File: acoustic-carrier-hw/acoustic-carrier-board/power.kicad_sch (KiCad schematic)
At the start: 73 parts, among them J201 Conn_02x06_Odd_Even, Q201 AO3401A, U201 TPS2121RUX, U202 TLV62569DBV, U203 TLV62569DBV, U204 TLV62569DBV, U205 TLV62569DBV, U206 OPA376xxDBV

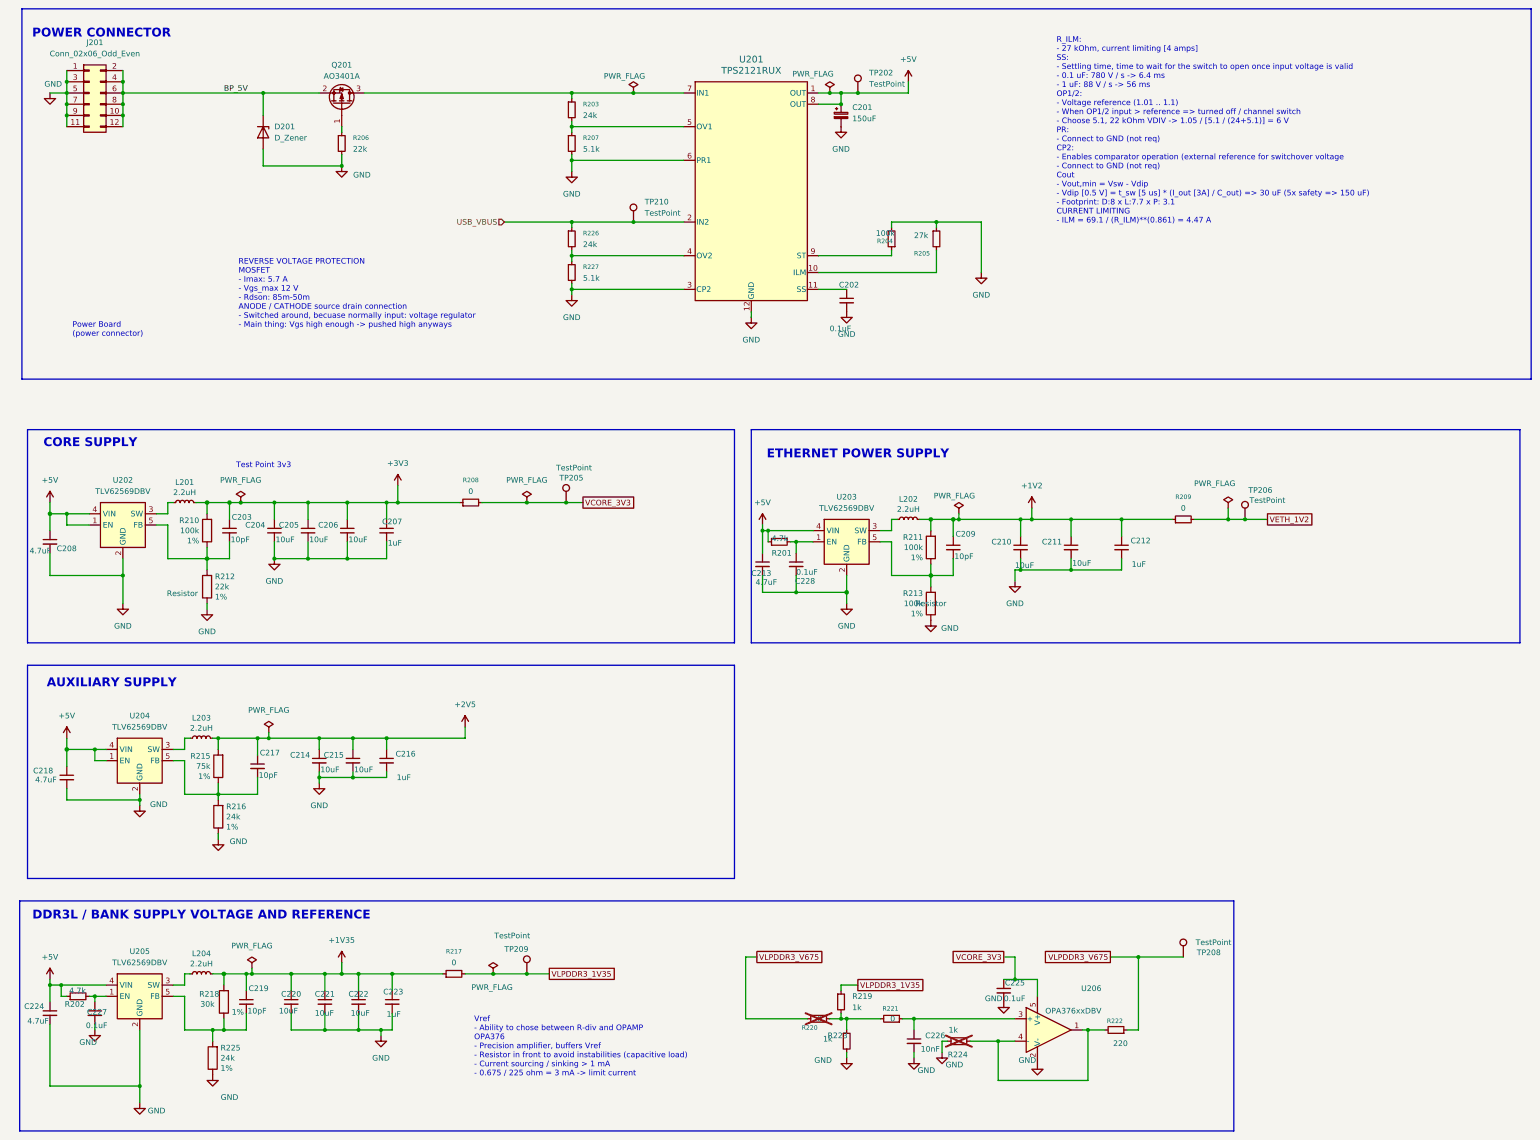
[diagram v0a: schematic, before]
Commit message: [carrier] finished for production (next) reroute the LPDDR3, with appropriate CMD-CTRL bus delays, and change banks for command-control
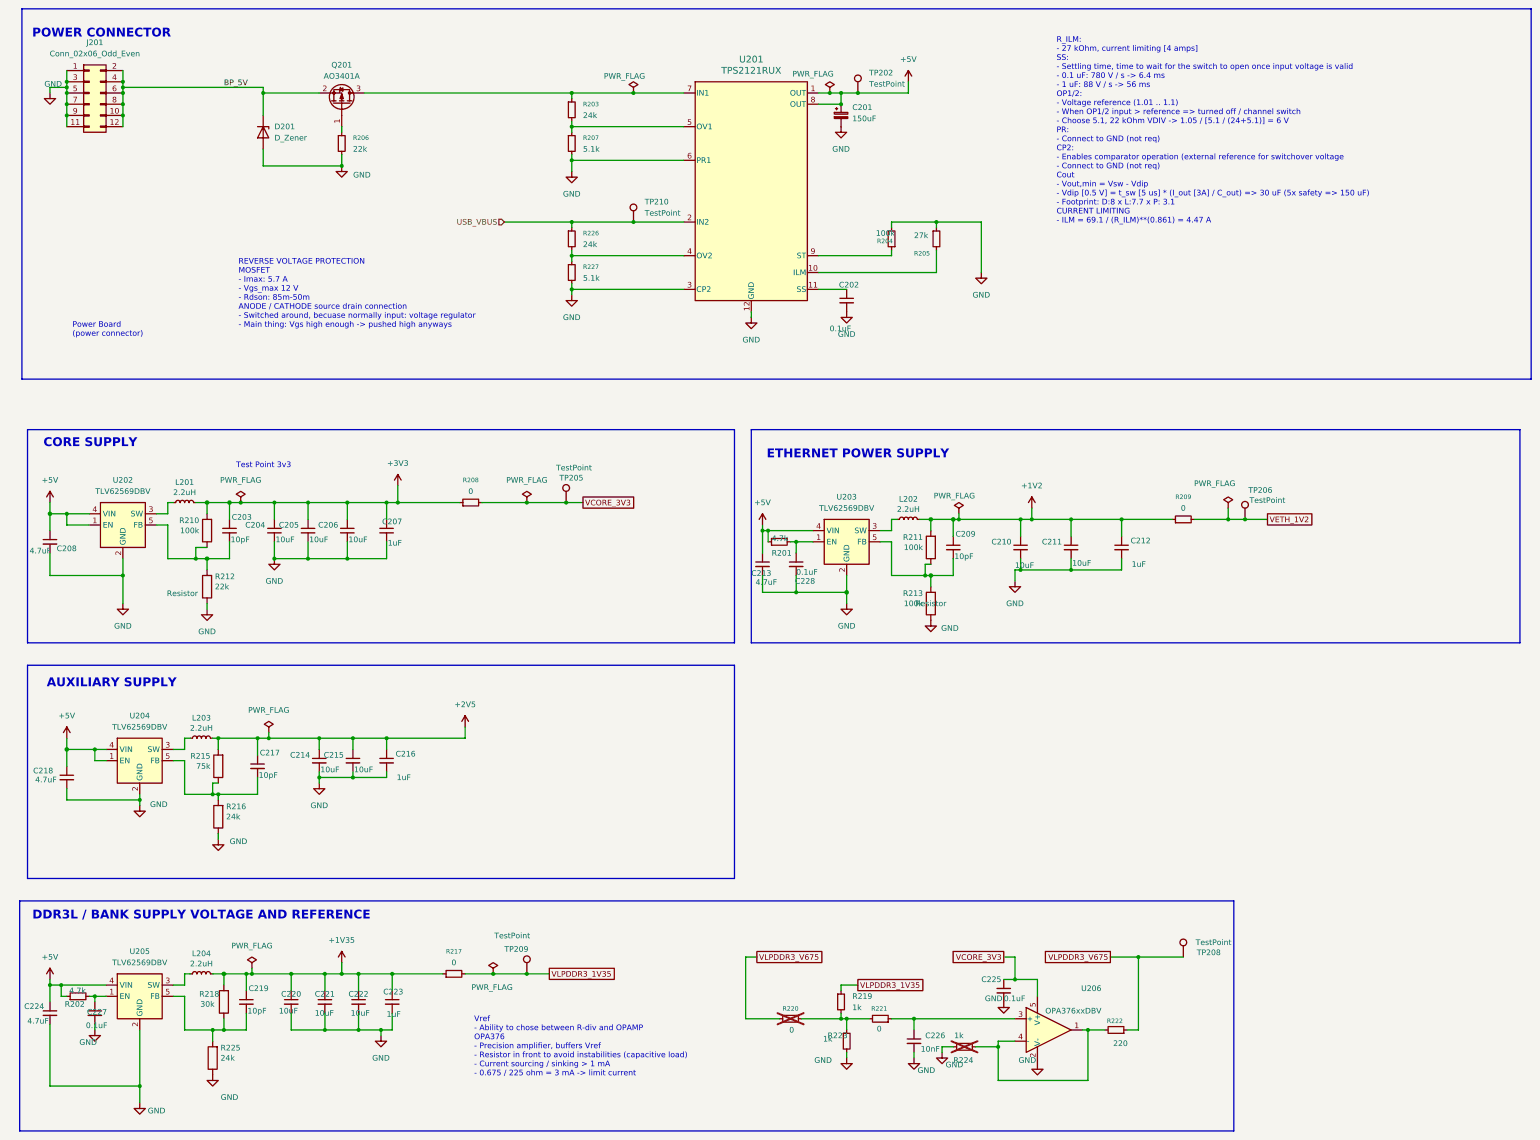
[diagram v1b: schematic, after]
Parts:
- R210, R211, R212, R213, R215, R216, R218, R225: Tol 1% -> (none)
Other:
- moved on the sheet: R220, R221, R224
